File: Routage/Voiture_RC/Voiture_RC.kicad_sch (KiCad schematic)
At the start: 28 parts, among them J1 Servomoteur, J2 Moteur, J3 NRF24L01, Q1 Q_PMOS_GSD, Q2 Q_NPN_BEC, Q3 FDS6681Z, Q4 FDS6681Z, Q5 FDS6681Z, Q6 FDS6681Z, U1 ESP32-WROOM-32, U2 AMS1117, U3 MCP1407-E/SN, U4 MCP1407-E/SN

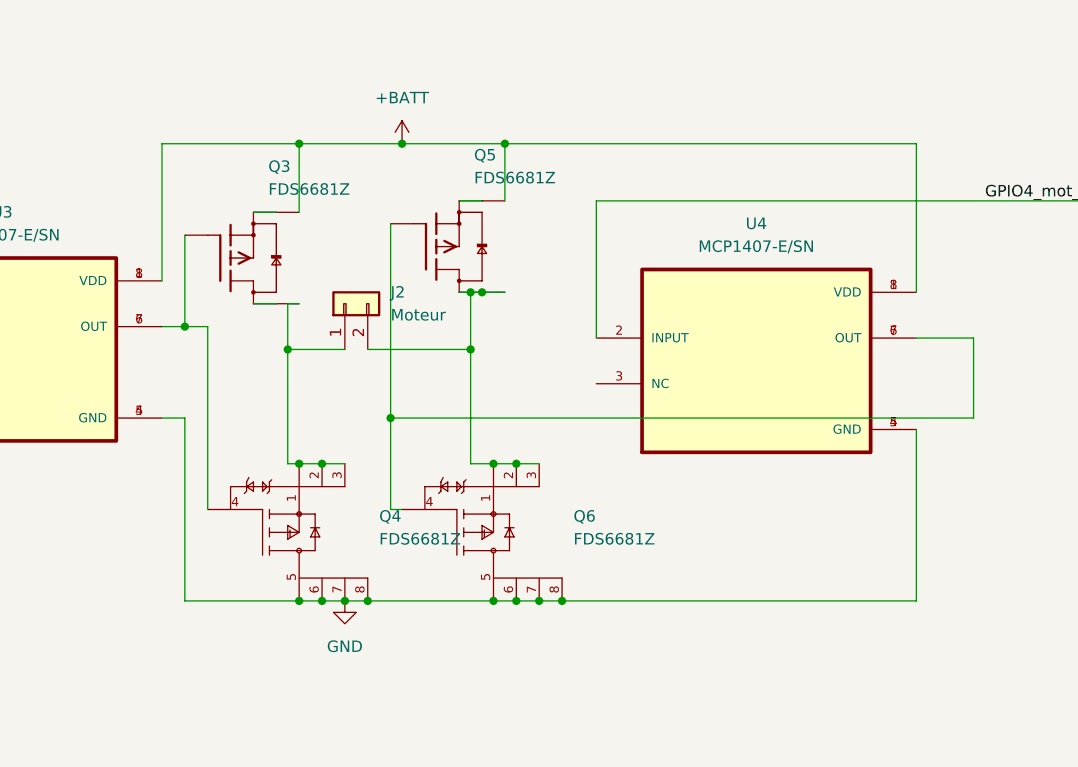
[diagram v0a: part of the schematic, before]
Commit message: Modification des mosfets avec les vrais symbols
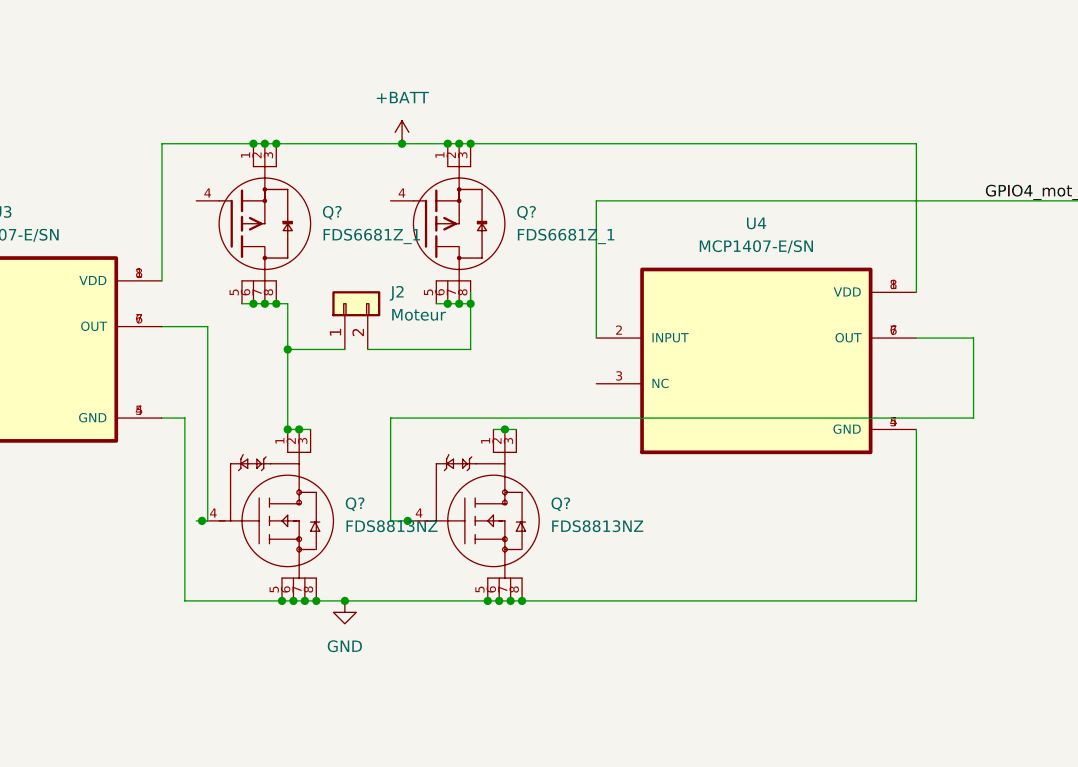
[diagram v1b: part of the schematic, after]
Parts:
- removed Q3, Q5: FDS6681Z, Package_SO:SOP-8_3.76x4.96mm_P1.27mm, symbol FDS6681Z_Mosfet_Puissance_canalP:FDS6681Z
- removed Q4, Q6: FDS6681Z, Package_SO:SOP-8_3.76x4.96mm_P1.27mm, symbol FDS8813NZ_Mosfet_Puissance_Canal_N:FDS6681Z
- added Q? (x2): FDS8813NZ, ON_Semi-751EB-08_2017-A-*, symbol FDS8813NZ:FDS8813NZ
- added Q? (x2): FDS6681Z_1, Package_SO:SOP-8_3.76x4.96mm_P1.27mm, symbol FDS6681Z:FDS6681Z_1
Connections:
- net +BATT: now also Q?.1, Q?.1, Q?.2, Q?.2, Q?.3, Q?.3
- net GND: now also Q?.5 (D), Q?.5 (D), Q?.6 (D), Q?.6 (D), Q?.7 (D), Q?.7 (D), Q?.8 (D), Q?.8 (D)
- net at U3.6 (OUT), U3.7 (OUT): now also Q?.4 (G)
- net at J2.1 (Pin_1): now also Q?.1 (S), Q?.2 (S), Q?.3 (S), Q?.5, Q?.6, Q?.7, Q?.8
- net at J2.2 (Pin_2): now also Q?.5, Q?.6, Q?.7, Q?.8
- net at U4.6 (OUT), U4.7 (OUT): now also Q?.4 (G)
- new net: Q?.1 (S), Q?.2 (S), Q?.3 (S)
